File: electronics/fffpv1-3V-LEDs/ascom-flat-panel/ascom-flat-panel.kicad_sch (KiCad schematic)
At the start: 12 parts, among them J1 Servo, J2 JST-XH LED, Q1 IRLZ34N, Q2 IRLZ34N, U1 XIAO-SAMD21-DIP

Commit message: [circuit] Schmetics update for 3V3 leds
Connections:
- net +3V3: now also J2.1 (Pin_1)
- net +5V: no longer J2.1 (Pin_1)
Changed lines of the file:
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@@
 	)
 	(symbol
-		(lib_name "+5V_1")
-		(lib_id "power:+5V")
+		(lib_id "power:+3V3")
 		(at 88.9 100.33 0)
 		(unit 1)
@@
 			)
 		)
-		(property "Value" "+5V"
+		(property "Value" "+3V3"
 			(at 88.9 95.25 0)
 			(effects
@@
 			)
 		)
-		(property "Description" "Power symbol creates a global label with name \"+5V\""
+		(property "Description" "Power symbol creates a global label with name \"+3V3\""
 			(at 88.9 100.33 0)
 			(effects

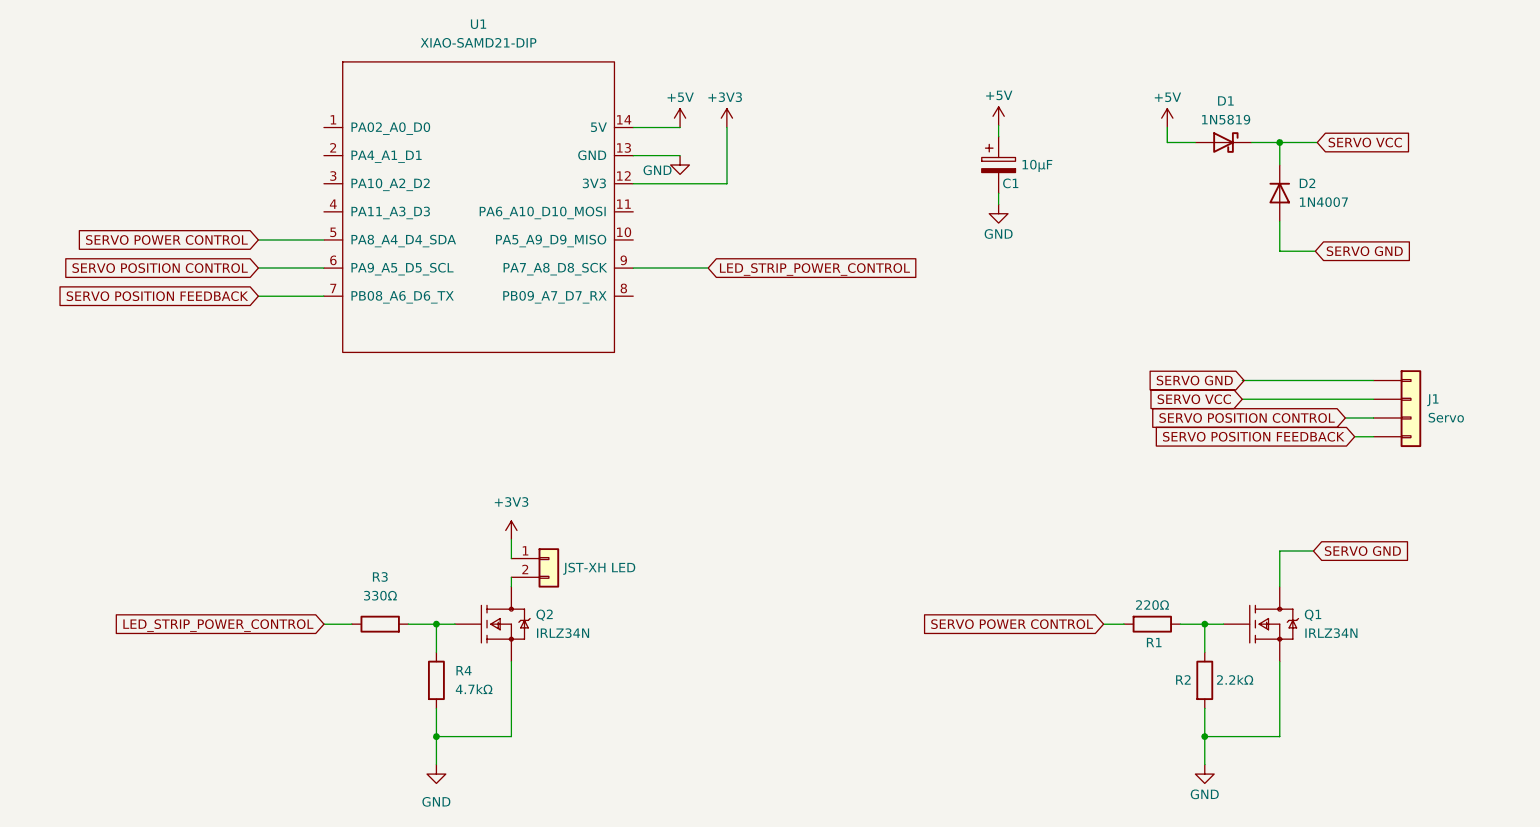
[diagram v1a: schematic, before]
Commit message: [circuit] Add decoupling capacitor betwenn +3V3 and GND
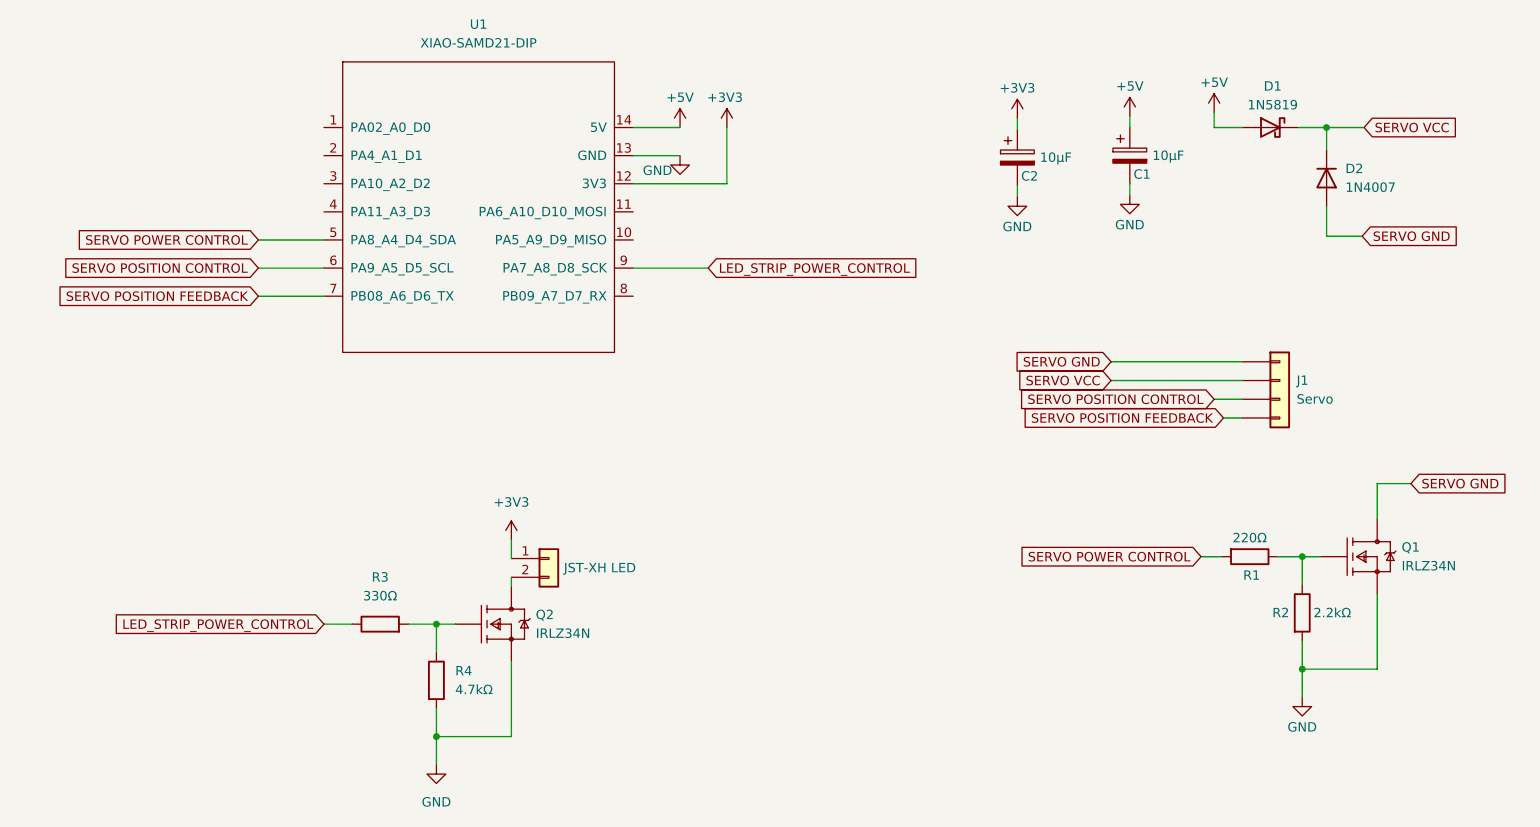
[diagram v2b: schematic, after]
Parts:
- added C2: 10µF, Capacitor_THT:C_Radial_D6.3mm_H11.0mm_P2.50mm, symbol Device:C_Polarized
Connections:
- net +3V3: now also C2.1
- net GND: now also C2.2
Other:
- moved on the sheet: C1, D1, D2, J1, Q1, R1, R2
